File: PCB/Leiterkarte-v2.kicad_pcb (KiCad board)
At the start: 4 copper layers, 88 parts, among them J1 MSD-1-A, SW33V1 Conn_01x01_Pin, U5V_StpDwn1 TPS5430DDA

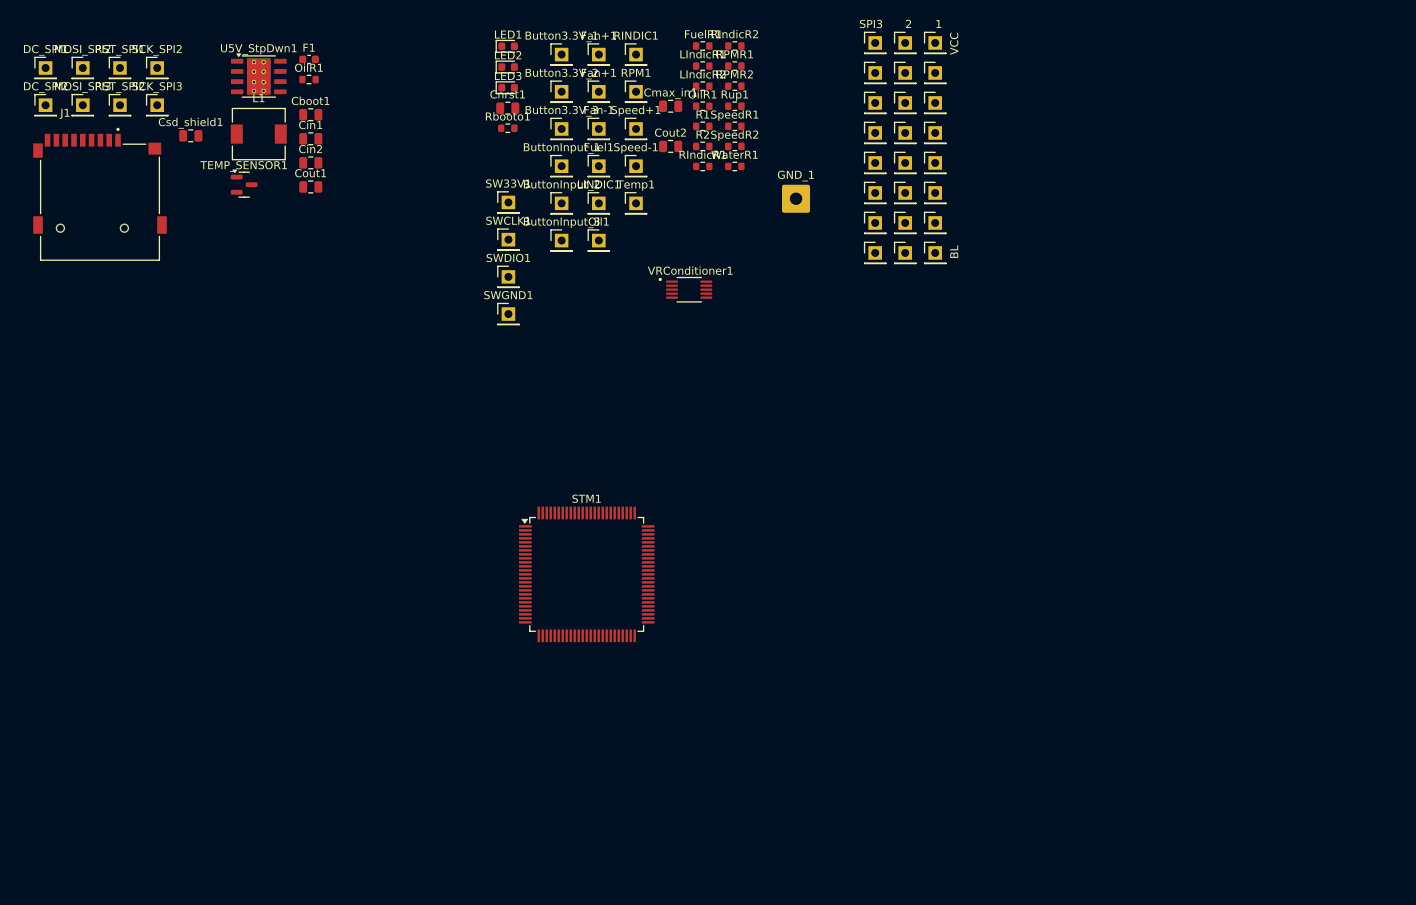
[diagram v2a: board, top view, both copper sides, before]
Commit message: Finalized circuit design; First try of PCB layout (FAILED)
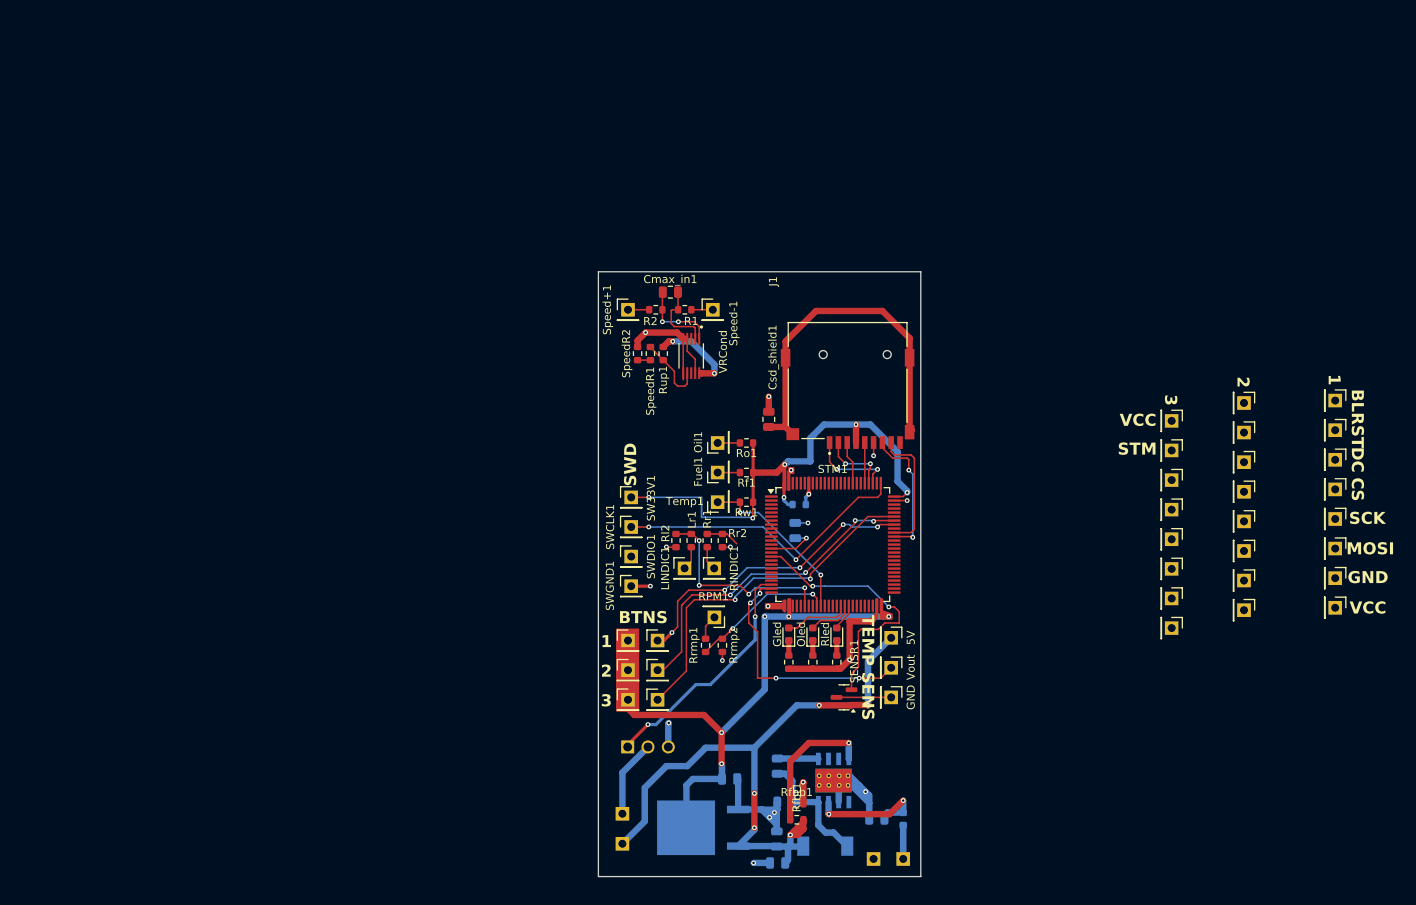
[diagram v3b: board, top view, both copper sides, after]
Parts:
- removed the DC_SPI1 at (75.3, 31.6)
- removed the DC_SPI1 at (182.8, 47.2)
- removed the DC_SPI2 at (75.3, 36.3)
- removed the DC_SPI2 at (179.0, 47.2)
- removed the Fan+1 at (144.5, 34.6)
- removed the Fan+1 at (144.5, 29.9)
- removed FuelR1, OilR1 (x2), WaterR1: 100, Resistor_SMD:R_0603_1608Metric
- removed GND_1: Conn_01x01_Pin, Connector_Wire:SolderWire-0.75sqmm_1x01_D1.25mm_OD3.5mm
- removed LED1: Green, LED_SMD:LED_0603_1608Metric
- removed LED2: Orange, LED_SMD:LED_0603_1608Metric
- removed LED3: Red, LED_SMD:LED_0603_1608Metric
- removed LIndicR1, RIndicR1, RPMR1: 40k, Resistor_SMD:R_0603_1608Metric
- removed LIndicR2, RIndicR2, RPMR2: 10k, Resistor_SMD:R_0603_1608Metric
- removed the MOSI_SPI2 at (186.5, 36.0)
- removed the MOSI_SPI2 at (80.0, 31.6)
- removed the MOSI_SPI3 at (80.0, 36.3)
- removed the MOSI_SPI3 at (182.8, 36.0)
- removed the RST_SPI1 at (182.8, 51.0)
- removed the RST_SPI1 at (84.6, 31.6)
- removed the RST_SPI2 at (84.6, 36.3)
- removed the RST_SPI2 at (179.0, 51.0)
- removed the SCK_SPI2 at (186.5, 39.8)
- removed the SCK_SPI2 at (89.2, 31.6)
- removed the SCK_SPI3 at (182.8, 39.8)
- removed the SCK_SPI3 at (89.2, 36.3)
- removed TEMP_SENSOR1: MCP9700Ax-ETT, Package_TO_SOT_SMD:SOT-23
- removed U5V_StpDwn1: TPS5430DDA, Package_SO:TI_SO-PowerPAD-8_ThermalVias
- removed VRConditioner1: MAX9924UAUB_T, MAX9924UAUB:SOP50P490X110-10N
- added 12V: Conn_01x01_Pin, Connector_PinHeader_2.54mm:PinHeader_1x01_P2.54mm_Vertical, B.Cu at (182.5, 130.5)
- added 3.3V_StpDwn1: NCV33269DTRK3.3G, NCV33269DTRK3.3G:DPAK-3_ONS-M, B.Cu at (155.4, 126.6)
- added 5V: Conn_01x01_Pin, Connector_PinHeader_2.54mm:PinHeader_1x01_P2.54mm_Vertical, F.Cu at (181.0, 102.9)
- added 5V_StpDwn1: TPS5430DDA, Package_SO:TI_SO-PowerPAD-8_ThermalVias, B.Cu at (173.8, 120.7)
- added D1: 550mV 5A, Diode_SMD:D_0805_2012Metric, B.Cu at (167.7, 123.4)
- added DC_SPI1: Conn_01x01_Pin, Connector_PinHeader_2.54mm:PinHeader_1x01_P2.54mm_Vertical, F.Cu at (236.5, 80.6)
- added DC_SPI2: Conn_01x01_Pin, Connector_PinHeader_2.54mm:PinHeader_1x01_P2.54mm_Vertical, F.Cu at (225.1, 80.9)
- added Fan+1: Conn_01x01_Pin, Connector_PinHeader_2.54mm:PinHeader_1x01_P2.54mm_Vertical, B.Cu at (147.4, 128.6)
- added GND: Conn_01x01_Pin, Connector_PinHeader_2.54mm:PinHeader_1x01_P2.54mm_Vertical, F.Cu at (181.0, 110.3)
- added GND: Conn_01x01_Pin, Connector_PinHeader_2.54mm:PinHeader_1x01_P2.54mm_Vertical, B.Cu at (178.8, 130.5)
- added Gled: Green, LED_SMD:LED_0603_1608Metric, F.Cu at (168.2, 102.4)
- added Lr1: 40k, Resistor_SMD:R_0603_1608Metric, F.Cu at (156.0, 90.7)
- added MOSI_SPI2: Conn_01x01_Pin, Connector_PinHeader_2.54mm:PinHeader_1x01_P2.54mm_Vertical, F.Cu at (225.1, 92.0)
- added MOSI_SPI3: Conn_01x01_Pin, Connector_PinHeader_2.54mm:PinHeader_1x01_P2.54mm_Vertical, F.Cu at (216.1, 94.2)
- added Oled: Orange, LED_SMD:LED_0603_1608Metric, F.Cu at (171.2, 102.4)
- added RST_SPI1: Conn_01x01_Pin, Connector_PinHeader_2.54mm:PinHeader_1x01_P2.54mm_Vertical, F.Cu at (236.5, 76.9)
- added RST_SPI2: Conn_01x01_Pin, Connector_PinHeader_2.54mm:PinHeader_1x01_P2.54mm_Vertical, F.Cu at (225.1, 77.2)
- added Rf1: 100, Resistor_SMD:R_0603_1608Metric, F.Cu at (162.9, 82.2)
- added Rfbb1: 3.24k, Resistor_SMD:R_0603_1608Metric, F.Cu at (169.2, 123.6)
- added Rfbt1: 10k, Resistor_SMD:R_0603_1608Metric, F.Cu at (169.2, 125.6)
- added Rl2: 10k, Resistor_SMD:R_0603_1608Metric, F.Cu at (154.1, 90.7)
- added Rled: Red, LED_SMD:LED_0603_1608Metric, F.Cu at (174.2, 102.4)
- added Rled1: 30, Resistor_SMD:R_0603_1608Metric, F.Cu at (168.2, 105.9)
- added Rled2: 150, Resistor_SMD:R_0603_1608Metric, F.Cu at (171.2, 105.9)
- added Rled3: 150, Resistor_SMD:R_0603_1608Metric, F.Cu at (174.2, 105.9)
- added Ro1: 100, Resistor_SMD:R_0603_1608Metric, F.Cu at (162.9, 78.5)
- added Rr1: 40k, Resistor_SMD:R_0603_1608Metric, F.Cu at (158.0, 90.7)
- added Rr2: 10k, Resistor_SMD:R_0603_1608Metric, F.Cu at (159.9, 90.7)
- added Rrmp1: 40k, Resistor_SMD:R_0603_1608Metric, F.Cu at (157.8, 103.8)
- added Rrmp2: 10k, Resistor_SMD:R_0603_1608Metric, F.Cu at (159.9, 103.8)
- added Rw1: 100, Resistor_SMD:R_0603_1608Metric, F.Cu at (162.9, 85.9)
- added SCK_SPI2: Conn_01x01_Pin, Connector_PinHeader_2.54mm:PinHeader_1x01_P2.54mm_Vertical, F.Cu at (225.1, 88.3)
- added SCK_SPI3: Conn_01x01_Pin, Connector_PinHeader_2.54mm:PinHeader_1x01_P2.54mm_Vertical, F.Cu at (216.1, 90.5)
- added SENSR1: MCP9700Ax-ETT, Package_TO_SOT_SMD:SOT-23, F.Cu at (175.1, 110.3)
- added U_fanmosfet1: IRL540NPBF, IRL540NPBF:PG-TO220-3_INF, B.Cu at (148.1, 116.5)
- added VRCond: MAX9924UAUB_T, MAX9924UAUB:SOP50P490X110-10N, F.Cu at (156.0, 67.6)
- added Vout: Conn_01x01_Pin, Connector_PinHeader_2.54mm:PinHeader_1x01_P2.54mm_Vertical, F.Cu at (181.0, 106.6)
- Cboot1, Cin1, Cin2, Cnrst1, Cout1, F1, Fan-1, L1, Rbooto1: moved to B.Cu
- Cout2: value 22uF -> 330uF; moved to B.Cu
- moved F1 120.5 mm to (182.5, 125.5), turned to 90 degrees
- moved L1 113.7 mm to (172.8, 128.9), turned to 180 degrees
- moved Cin1 110.6 mm to (179.2, 125.5), turned to 180 degrees
- moved Cin2 105.2 mm to (166.8, 131.0), turned to 180 degrees
- moved Cboot1 100.2 mm to (166.8, 118.9), turned to 90 degrees
- moved J1 96.1 mm to (175.6, 70.7), turned to 180 degrees
- moved VCC_SPI_1 91.1 mm to (236.5, 99.1), turned to -90 degrees
- moved Cout1 90.6 mm to (160.8, 120.5), turned to 180 degrees
- moved Cout2 87.6 mm to (166.7, 128.0), turned to 90 degrees
- moved Fan-1 85.7 mm to (147.4, 124.8), turned to 90 degrees
- moved GND_SPI_1 85.4 mm to (236.5, 95.4), turned to -90 degrees
- moved VCC_SPI_2 82.6 mm to (225.1, 99.4), turned to -90 degrees
- moved Csd_shield1 80.5 mm to (165.7, 75.5), turned to -90 degrees
- moved MOSI_SPI1 80.1 mm to (236.5, 91.7), turned to -90 degrees
- moved VCC_SPI_3 78.9 mm to (216.1, 101.6), turned to -90 degrees
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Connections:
- Cout2 pad 1: 5V -> +5V
- Fan-1 pad 1: GND -> Net-(Fan-1-Pin_1)
- STM1 pad 22: unconnected-(STM1-PA0-Pad22) -> Net-(BL_SPI1-Pin_1)
- STM1 pad 23: unconnected-(STM1-PA1-Pad23) -> FANCTRL
- STM1 pad 28: Net-(BL_SPI1-Pin_1) -> unconnected-(STM1-PA4-Pad28)
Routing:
- net +3.3V: track 0.00 -> 126.1 mm, vias 0 -> 11
- net GND: track 0.00 -> 93.9 mm, vias 0 -> 18
- net +5V: track 0.00 -> 91.6 mm, vias 0 -> 7
- net Net-(Csd_shield1-Pad2): track 0.00 -> 44.7 mm
- net Button3: track 0.00 -> 44.4 mm, vias 0 -> 2
- net Button2: track 0.00 -> 41.0 mm, vias 0 -> 4
- net Button1: track 0.00 -> 37.7 mm, vias 0 -> 5
- net SWCLK: track 0.00 -> 37.7 mm, vias 0 -> 2
- net TEMP1: track 0.00 -> 33.4 mm, vias 0 -> 2
- net TEMP2: track 0.00 -> 30.8 mm, vias 0 -> 4
- net FANCTRL: track 0.00 -> 30.2 mm, vias 0 -> 2
- net LIndicator: track 0.00 -> 25.1 mm, vias 0 -> 4
- net WTemp: track 0.00 -> 21.3 mm, vias 0 -> 2
- net RPM: track 0.00 -> 18.1 mm, vias 0 -> 2
- net Net-(5V_StpDwn1-VSENSE): track 0.00 -> 17.6 mm, vias 0 -> 1
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- added copper zone on In1.Cu, net GND
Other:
- board outline added: 40.3 x 75.6 mm
- board text added: "3"
- board text added: "BTNS"
- board text added: "CS"
- board text added: "DC"
- board text added: "GND"
- board text added: "MOSI"
- board text added: "RST"
- board text added: "SCK"
- board text added: "STM"
- board text added: "SWD"
- board text added: "TEMP SENS"
- board text removed: "SPI3"

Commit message: Finalized circuit design; Added PCB layout
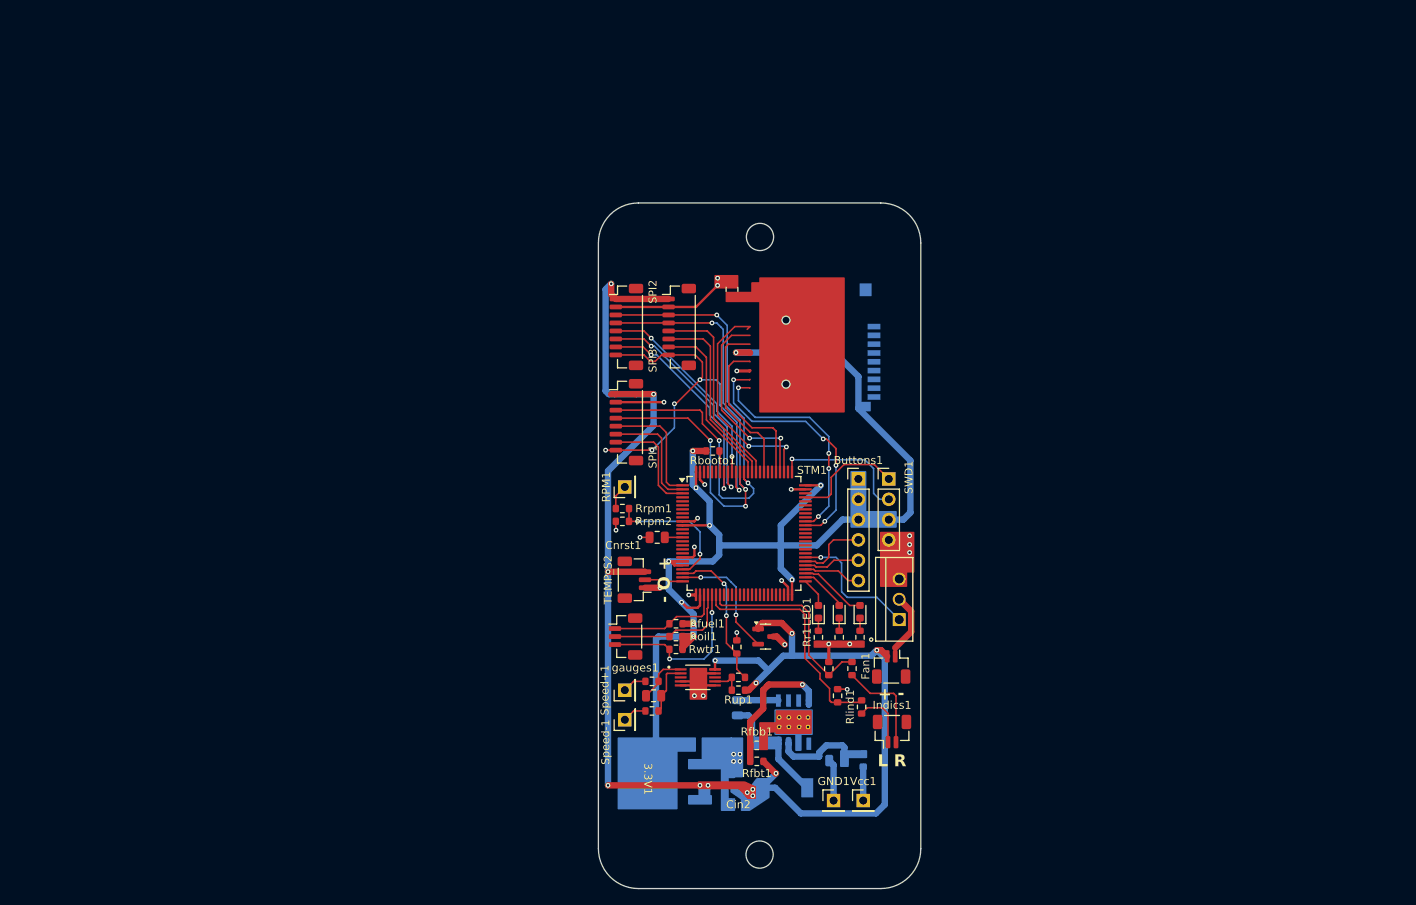
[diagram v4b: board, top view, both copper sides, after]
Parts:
- removed 3.3V_StpDwn1: NCV33269DTRK3.3G, NCV33269DTRK3.3G:DPAK-3_ONS-M
- removed 5V, BL_SPI1, BL_SPI2, BL_SPI3, Button3.3V_1, Button3.3V_2, Button3.3V_3, ButtonInput_1, ButtonInput_2, ButtonInput_3, CS_SPI1, CS_SPI2, CS_SPI3, DC_SPI1, DC_SPI2, DC_SPI3, Fan+1, Fan-1, Fuel1, GND, GND_SPI_1, GND_SPI_2, GND_SPI_3, LINDIC1, MOSI_SPI1, MOSI_SPI2, MOSI_SPI3, Oil1, RINDIC1, RST_SPI1, RST_SPI2, RST_SPI3, SCK_SPI1, SCK_SPI2, SCK_SPI3, SW33V1, SWCLK1, SWDIO1, SWGND1, Temp1, VCC_SPI_1, VCC_SPI_2, VCC_SPI_3, Vout: Conn_01x01_Pin, Connector_PinHeader_2.54mm:PinHeader_1x01_P2.54mm_Vertical
- removed Cmax_in1: 1nF, Capacitor_SMD:C_0805_2012Metric
- removed Gled: Green, LED_SMD:LED_0603_1608Metric
- removed Lr1, Rrmp1: 40k, Resistor_SMD:R_0603_1608Metric
- removed Oled: Orange, LED_SMD:LED_0603_1608Metric
- removed Rf1, Rw1: 100, Resistor_SMD:R_0603_1608Metric
- removed Rl2, Rr2, Rrmp2, SpeedR1: 10k, Resistor_SMD:R_0603_1608Metric
- removed Rled: Red, LED_SMD:LED_0603_1608Metric
- removed Rled1: 30, Resistor_SMD:R_0603_1608Metric
- removed Rled2, Rled3: 150, Resistor_SMD:R_0603_1608Metric
- removed SENSR1: MCP9700Ax-ETT, Package_TO_SOT_SMD:SOT-23
- removed SpeedR2: 20k, Resistor_SMD:R_0603_1608Metric
- removed U_fanmosfet1: IRL540NPBF, IRL540NPBF:PG-TO220-3_INF
- removed VRCond: MAX9924UAUB_T, MAX9924UAUB:SOP50P490X110-10N
- added 3.3V1: NCV33269DTRK3.3G, NCV33269DTRK3.3G:DPAK-3_ONS-M, B.Cu at (150.6, 120.8)
- added Buttons1: Conn_01x06_Pin, Connector_PinHeader_2.54mm:PinHeader_1x06_P2.54mm_Vertical, F.Cu at (176.9, 83.0)
- added Cmax1: 1nF, Capacitor_SMD:C_0805_2012Metric, F.Cu at (151.3, 110.1)
- added Fan1: Conn_01x02_Pin, Connector_JST:JST_SH_BM02B-SRSS-TB_1x02-1MP_P1.00mm_Vertical, F.Cu at (181.0, 106.5)
- added Indics1: Conn_01x02_Pin, Connector_JST:JST_SH_BM02B-SRSS-TB_1x02-1MP_P1.00mm_Vertical, F.Cu at (181.1, 114.6)
- added LED1: Red, LED_SMD:LED_0603_1608Metric, F.Cu at (171.9, 99.6)
- added LED2: Orange, LED_SMD:LED_0603_1608Metric, F.Cu at (174.5, 99.6)
- added LED3: Green, LED_SMD:LED_0603_1608Metric, F.Cu at (177.1, 99.6)
- added Rfuel1: 100, Resistor_SMD:R_0603_1608Metric, F.Cu at (154.1, 101.1)
- added Rg1: 30, Resistor_SMD:R_0603_1608Metric, F.Cu at (177.1, 102.8)
- added Rlind1: 40k, Resistor_SMD:R_0603_1608Metric, F.Cu at (177.3, 111.5)
- added Rlind2: 10k, Resistor_SMD:R_0603_1608Metric, F.Cu at (174.3, 110.1)
- added Roil1: 100, Resistor_SMD:R_0603_1608Metric, F.Cu at (154.1, 102.7)
- added Rrind1: 40k, Resistor_SMD:R_0603_1608Metric, F.Cu at (176.1, 106.7)
- added Rrind2: 10k, Resistor_SMD:R_0603_1608Metric, F.Cu at (173.2, 106.7)
- added Rrpm1: 40k, Resistor_SMD:R_0603_1608Metric, F.Cu at (147.4, 86.7)
- added Rrpm2: 10k, Resistor_SMD:R_0603_1608Metric, F.Cu at (147.4, 88.3)
- added Rspd1: 10k, Resistor_SMD:R_0603_1608Metric, F.Cu at (161.9, 107.8)
- added Rspd2: 20k, Resistor_SMD:R_0603_1608Metric, F.Cu at (161.7, 104.0)
- added Rwtr1: 100, Resistor_SMD:R_0603_1608Metric, F.Cu at (154.1, 104.3)
- added SPI1: Conn_01x08, Connector_JST:JST_SH_BM08B-SRSS-TB_1x08-1MP_P1.00mm_Vertical, F.Cu at (147.9, 75.9)
- added SPI2: Conn_01x08, Connector_JST:JST_SH_BM08B-SRSS-TB_1x08-1MP_P1.00mm_Vertical, F.Cu at (147.9, 64.0)
- added SPI3: Conn_01x08, Connector_JST:JST_SH_BM08B-SRSS-TB_1x08-1MP_P1.00mm_Vertical, F.Cu at (154.5, 64.0)
- added SWD1: Conn_01x04_Pin, Connector_PinHeader_2.54mm:PinHeader_1x04_P2.54mm_Vertical, F.Cu at (180.7, 83.0)
- added TEMP_S1: MCP9700Ax-ETT, Package_TO_SOT_SMD:SOT-23, F.Cu at (165.3, 102.7)
- added TEMP_S2: Conn_01x03_Pin, Connector_JST:JST_SH_BM03B-SRSS-TB_1x03-1MP_P1.00mm_Vertical, F.Cu at (148.9, 95.6)
- added Ufan1: IRL540NPBF, IRL540NPBF:PG-TO220-3_INF, F.Cu at (182.0, 100.6)
- added VRCond1: MAX9924UAUB_T, MAX9924UAUB:SOP50P490X110-10N, F.Cu at (156.8, 107.8)
- added gauges1: Conn_01x03_Pin, Connector_JST:JST_SH_BM03B-SRSS-TB_1x03-1MP_P1.00mm_Vertical, F.Cu at (147.8, 102.7)
- Cnrst1, Rbooto1: moved to F.Cu
- GND1: renamed from GND; moved to F.Cu
- Ro1: value 100 -> 150
- Rr1: value 40k -> 150
- SD1: renamed from J1; moved to B.Cu
- Vcc1: renamed from 12V; moved to F.Cu
- moved Speed-1 52.4 mm to (147.7, 113.1), turned to 90 degrees
- moved R1 50.3 mm to (151.1, 112.0), turned to 0 degrees
- moved Speed+1 47.6 mm to (147.7, 109.4), turned to 90 degrees
- moved R2 46.5 mm to (151.1, 108.3)
- moved Rup1 43.1 mm to (161.9, 109.4), turned to 0 degrees
- moved Ro1 26.9 mm to (174.5, 102.8), turned to 90 degrees
- moved RPM1 19.7 mm to (147.7, 84.0), turned to 90 degrees
- moved Rr1 18.4 mm to (171.9, 102.8)
- moved Cnrst1 17.3 mm to (151.8, 90.3), turned to 180 degrees
- moved Cshld1 16.9 mm to (161.1, 59.3)
- moved Rbooto1 12.7 mm to (158.7, 79.5)
- moved STM1 11.2 mm to (162.6, 89.8)
- moved Cboot1 8.85 mm to (161.8, 111.6)
- moved D1 8.85 mm to (162.7, 116.1)
- moved L1 8.85 mm to (167.8, 121.6)
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- renumbered 5V_StpDwn1 to 5V1, Csd_shield1 to Cshld1
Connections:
- Ro1 pad 1: +3.3V -> GND
- Ro1 pad 2: Oil -> Net-(LED2-K)
- Rr1 pad 1: Net-(RINDIC1-Pin_1) -> GND
- Rr1 pad 2: RIndicator -> Net-(LED1-K)
- STM1 pad 1: Net-(CS_SPI1-Pin_1) -> CS1
- STM1 pad 15: Speed -> unconnected-(STM1-PC0-Pad15)
- STM1 pad 16: TEMP1 -> unconnected-(STM1-PC1-Pad16)
- STM1 pad 18: Net-(MOSI_SPI3-Pin_1) -> unconnected-(STM1-PC3_C-Pad18)
- STM1 pad 2: Net-(CS_SPI2-Pin_1) -> DC1
- STM1 pad 22: Net-(BL_SPI1-Pin_1) -> RPM
- STM1 pad 23: FANCTRL -> Speed
- STM1 pad 24: TEMP2 -> TEMP1
- STM1 pad 25: unconnected-(STM1-PA3-Pad25) -> TEMP2
- STM1 pad 28: unconnected-(STM1-PA4-Pad28) -> Fuel
- STM1 pad 29: Net-(SCK_SPI1-Pin_1) -> Oil
- STM1 pad 3: Net-(CS_SPI3-Pin_1) -> RST1
- STM1 pad 30: Fuel -> WTemp
- STM1 pad 32: Oil -> RIndicator
- STM1 pad 33: RIndicator -> unconnected-(STM1-PC5-Pad33)
- STM1 pad 34: RPM -> unconnected-(STM1-PB0-Pad34)
- STM1 pad 35: WTemp -> unconnected-(STM1-PB1-Pad35)
- STM1 pad 36: Net-(MOSI_SPI2-Pin_1) -> unconnected-(STM1-PB2-Pad36)
- STM1 pad 40: Net-(LED1-A) -> unconnected-(STM1-PE10-Pad40)
- STM1 pad 41: Net-(LED2-A) -> unconnected-(STM1-PE11-Pad41)
- STM1 pad 42: Net-(LED3-A) (its old number) -> unconnected-(STM1-PE12-Pad42)
- STM1 pad 46: Net-(SCK_SPI3-Pin_1) -> unconnected-(STM1-PB10-Pad46)
- STM1 pad 51: unconnected-(STM1-PB12-Pad51) -> Net-(LED1-A)
- STM1 pad 52: unconnected-(STM1-PB13-Pad52) -> Net-(LED2-A)
- STM1 pad 54: Net-(DC_SPI3-Pin_1) -> Button3
- STM1 pad 55: unconnected-(STM1-PD8-Pad55) -> Button2
- STM1 pad 56: unconnected-(STM1-PD9-Pad56) -> Button1
- STM1 pad 57: unconnected-(STM1-PD10-Pad57) -> FANCTRL
- STM1 pad 58: Net-(RST_SPI1-Pin_1) -> unconnected-(STM1-PD11-Pad58)
- STM1 pad 59: Net-(DC_SPI1-Pin_1) -> unconnected-(STM1-PD12-Pad59)
- STM1 pad 61: Net-(RST_SPI2-Pin_1) -> unconnected-(STM1-PD14-Pad61)
- STM1 pad 62: Net-(DC_SPI2-Pin_1) -> unconnected-(STM1-PD15-Pad62)
- STM1 pad 68: Button1 -> unconnected-(STM1-PA9-Pad68)
- STM1 pad 69: Button2 -> unconnected-(STM1-PA10-Pad69)
- STM1 pad 70: Button3 -> unconnected-(STM1-PA11-Pad70)
- STM1 pad 85: unconnected-(STM1-PD4-Pad85) -> CS3
- STM1 pad 86: unconnected-(STM1-PD5-Pad86) -> DC3
- STM1 pad 87: unconnected-(STM1-PD6-Pad87) -> RST3
- STM1 pad 88: Net-(MOSI_SPI1-Pin_1) -> DIN
- STM1 pad 89: Net-(SCK_SPI2-Pin_1) -> CLK
- STM1 pad 90: unconnected-(STM1-PB4-Pad90) -> BL
- STM1 pad 91: unconnected-(STM1-PB5-Pad91) -> CS2
- STM1 pad 92: unconnected-(STM1-PB6-Pad92) -> DC2
- STM1 pad 93: unconnected-(STM1-PB7-Pad93) -> RST2
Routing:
- net +5V: track 91.6 -> 180.5 mm, vias 7 -> 14
- net DIN: track 0.00 -> 65.2 mm, vias 0 -> 3
- net CLK: track 0.00 -> 64.1 mm, vias 0 -> 4
- net BL: track 0.00 -> 51.6 mm, vias 0 -> 5
- net Net-(Cshld1-Pad2): track 44.7 -> 0.00 mm
- net Button3: track 44.4 -> 7.20 mm, vias 2 -> 0
- net Button2: track 41.0 -> 7.06 mm, vias 4 -> 0
- net GND: track 93.9 -> 60.2 mm, vias 18 -> 27
- net +3.3V: track 126.1 -> 155.6 mm, vias 11 -> 10
- net Button1: track 37.7 -> 8.84 mm, vias 5 -> 0
- net DC2: track 0.00 -> 28.8 mm, vias 0 -> 2
- net RST2: track 0.00 -> 27.8 mm, vias 0 -> 2
- net TEMP2: track 30.8 -> 4.78 mm, vias 4 -> 0
- net CS2: track 0.00 -> 25.7 mm, vias 0 -> 2
- net CS3: track 0.00 -> 25.0 mm
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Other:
- board size 40.3 x 75.6 mm -> 40.3 x 85.7 mm
- board text added: "- +"
- board text added: "- O +"
- board text added: "F O W"
- board text added: "L R"
- board text removed: "1"
- board text removed: "2"
- board text removed: "3"
- board text removed: "BL"
- board text removed: "BTNS"
- board text removed: "CS"
- board text removed: "DC"
- board text removed: "GND"
- board text removed: "MOSI"
- board text removed: "RST"
- board text removed: "SCK"
- board text removed: "STM"
- board text removed: "SWD"
- board text removed: "TEMP SENS"
- board text removed: "VCC"
